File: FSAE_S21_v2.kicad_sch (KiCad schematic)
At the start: 56 parts

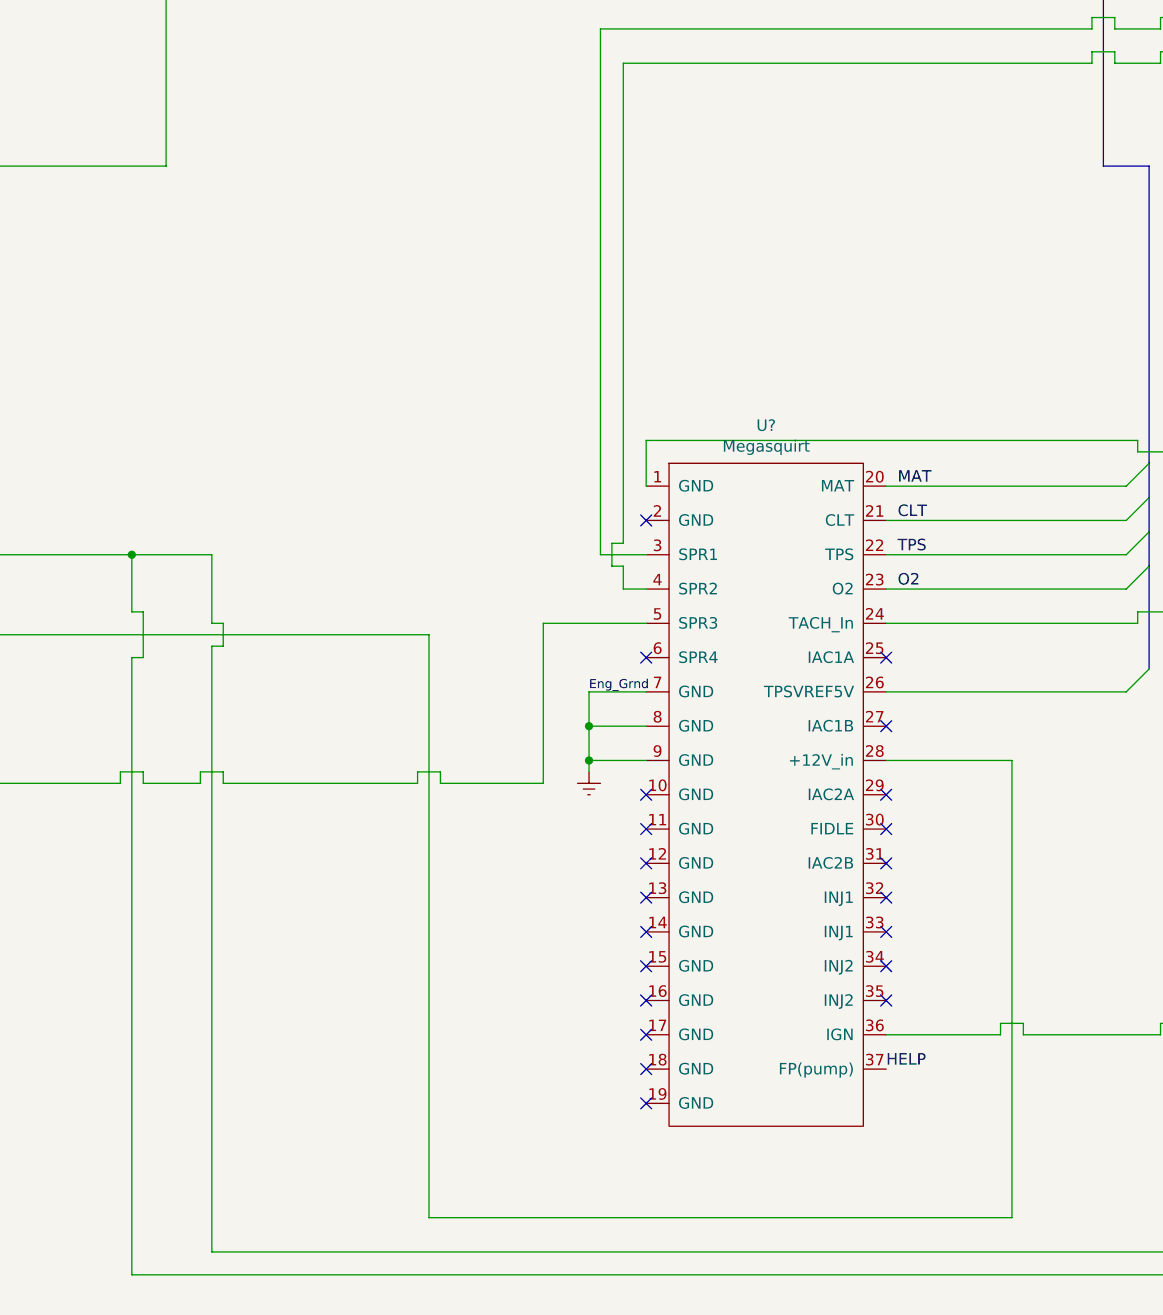
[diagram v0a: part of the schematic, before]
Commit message: Fixing pin 37
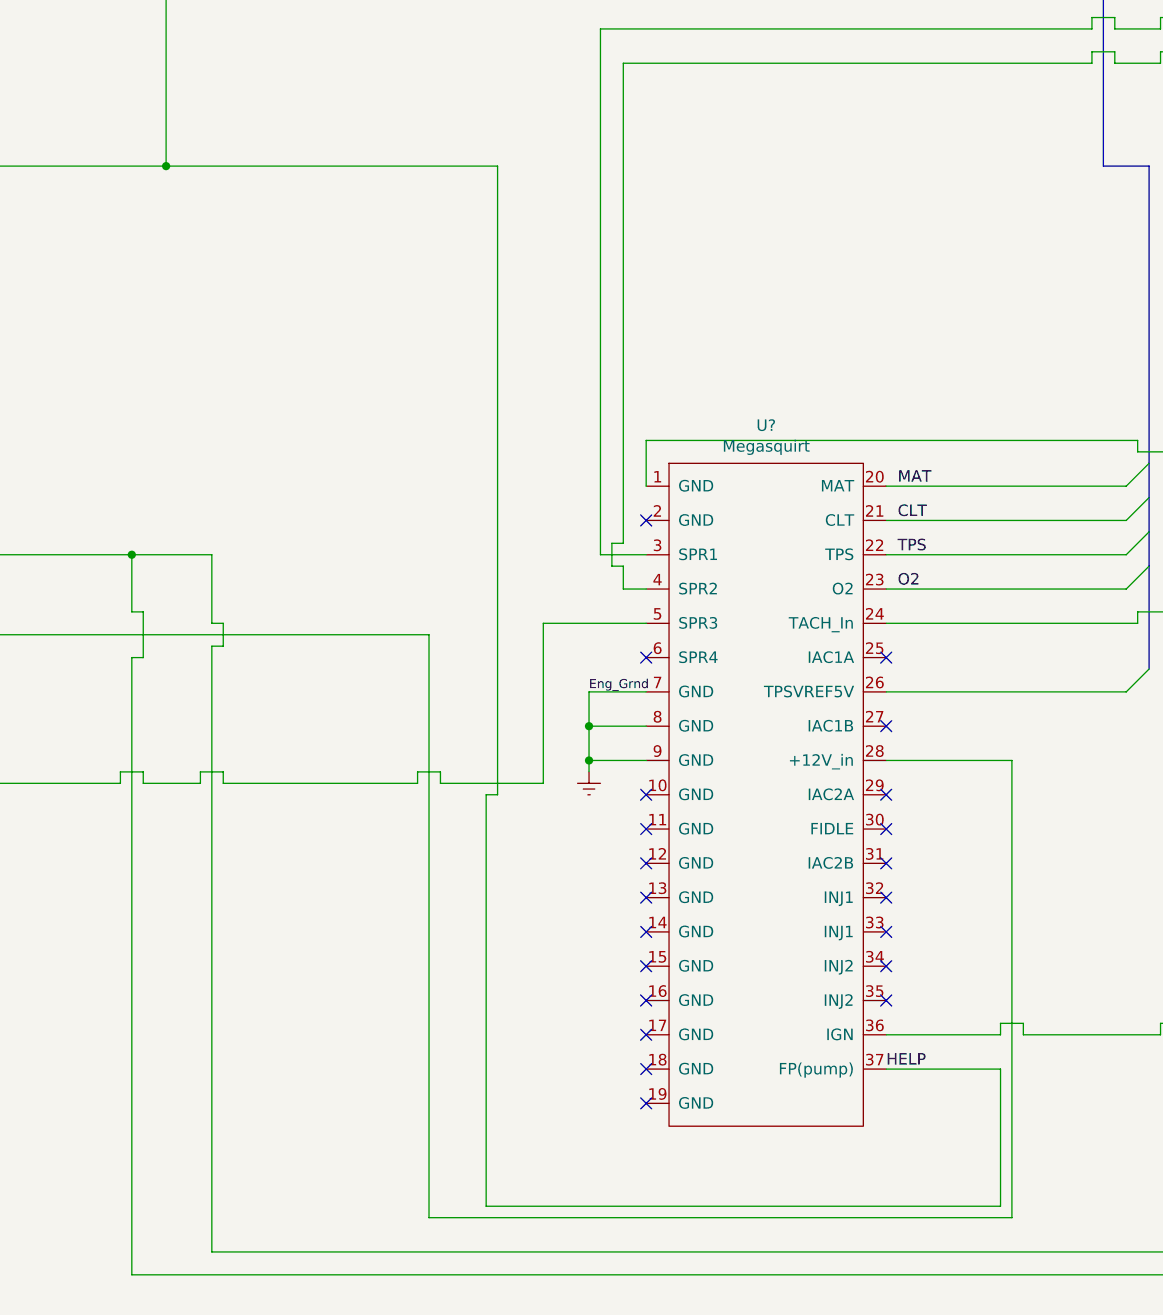
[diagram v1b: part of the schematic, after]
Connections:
- net HELP: now also SW?.2 (B)
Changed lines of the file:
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@@
   (junction (at 419.1 222.25) (diameter 0) (color 0 0 0 0)
+  )
+  (junction (at 251.46 130.81) (diameter 0) (color 0 0 0 0)
   )
   (junction (at 180.34 111.76) (diameter 0) (color 0 0 0 0)
@@
     (stroke (width 0) (type default) (color 0 0 0 0))
   )
+  (wire (pts (xy 331.47 231.14) (xy 344.17 231.14))
+    (stroke (width 0) (type default) (color 0 0 0 0))
+  )
   (bus (pts (xy 207.01 30.48) (xy 207.01 33.02))
     (stroke (width 0) (type default) (color 0 0 0 0))
@@
     (stroke (width 0) (type default) (color 0 0 0 0))
   )
+  (wire (pts (xy 287.02 200.66) (xy 288.29 200.66))
+    (stroke (width 0) (type default) (color 0 0 0 0))
+  )
   (wire (pts (xy 420.37 43.18) (xy 422.91 43.18))
     (stroke (width 0) (type default) (color 0 0 0 0))
@@
     (stroke (width 0) (type default) (color 0 0 0 0))
   )
+  (wire (pts (xy 344.17 246.38) (xy 287.02 246.38))
+    (stroke (width 0) (type default) (color 0 0 0 0))
+  )
   (wire (pts (xy 151.13 73.66) (xy 151.13 81.28))
     (stroke (width 0) (type default) (color 0 0 0 0))
@@
     (stroke (width 0) (type default) (color 0 0 0 0))
   )
+  (wire (pts (xy 288.29 130.81) (xy 288.29 200.66))
+    (stroke (width 0) (type default) (color 0 0 0 0))
+  )
   (wire (pts (xy 182.88 21.59) (xy 78.74 21.59))
     (stroke (width 0) (type default) (color 0 0 0 0))
@@
     (stroke (width 0) (type default) (color 0 0 0 0))
   )
+  (wire (pts (xy 344.17 231.14) (xy 344.17 246.38))
+    (stroke (width 0) (type default) (color 0 0 0 0))
+  )
   (wire (pts (xy 219.71 74.93) (xy 222.25 74.93))
     (stroke (width 0) (type default) (color 0 0 0 0))
@@
     (stroke (width 0) (type default) (color 0 0 0 0))
   )
+  (wire (pts (xy 287.02 246.38) (xy 287.02 200.66))
+    (stroke (width 0) (type default) (color 0 0 0 0))
+  )
   (wire (pts (xy 497.84 138.43) (xy 511.81 138.43))
     (stroke (width 0) (type default) (color 0 0 0 0))
@@
     (stroke (width 0) (type default) (color 0 0 0 0))
   )
+  (wire (pts (xy 288.29 130.81) (xy 251.46 130.81))
+    (stroke (width 0) (type default) (color 0 0 0 0))
+  )

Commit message: Some fixes
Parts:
- removed F?: Fuse (5 A), symbol Device:Fuse
- removed J?: ICM, symbol Connector:DB9_Female
- removed J?: MyChron 5 (EXP/PC), symbol Connector:DIN-5
- removed SW?: Starter Button, symbol Switch:SW_MEC_5G
- removed U?: IC1, symbol Device:IC
- removed U?: IC2, symbol Device:IC
- removed U?: IC3, symbol Device:IC
- removed U?: IC4, symbol Device:IC
- added J?: ICM, symbol Connector:DB9_Female
- added R?: 10k, symbol Device:R_US
- added SW?: Datalog Button, symbol Switch:SW_Push
- added SW?: Upshift Button, symbol Switch:SW_Push
- added SW?: Starter Button, symbol Switch:SW_MEC_5G
- added SW?: Downshift Button, symbol Switch:SW_Push
- added SW?: TC Button, symbol Switch:SW_Push
- added U?: IC3, symbol Device:IC
- added U?: IC2, symbol Device:IC
- added U?: DSS, symbol Device:IC
- added U?: IC4, symbol Device:IC
- added U?: USS, symbol Device:IC
- added U?: IC1, symbol Device:IC
- F?: value Fuse (????? A) -> Fuse (5 A)
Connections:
- net 12V: no longer F?.1, U?.1 (+12V_In)
- net Earth: now also U?.2 (GND), U?.3 (GND), J?.3, SW?.1, SW?.1 (A), SW?.2, SW?.2, SW?.2, SW?.2 (A); no longer K?.3, U?.35 (Spark_E)
- net TracCtrl: now also SW?.2
- net V_CKS: now also K?.5
- net V_PKS: now also U?.~ (VCC), U?.~ (VCC)
- net at F?.1: now also U?.~ (VCC), U?.~ (VCC), U?.~ (VCC), U?.~ (VCC)
- net at J?.2 (Pin_2): now also R?.2
- net at U?.24 (TACH_In): now also R?.1
- net at U?.30 (Datalog_in): now also SW?.1
- net Dshift_button renamed DS_Button
- net DS_Button: now also SW?.1
- net OPS renamed Oil Pres.
- net Oil Pres.: no longer U?.2 (IO)
- net OTS renamed Oil Temp
- net Ushift_button renamed US_Button
- net US_Button: now also SW?.1
- new net: K?.3, SW?.3 (B), SW?.4 (B)
- new net: F?.1, U?.1 (+12V_In)
- new net: J?.7, U?.~ (VCC)
- new net: J?.8, U?.~ (VCC)
- new net: J?.6, U?.~ (VCC)
- new net: J?.9, U?.~ (VCC)
- new net DS Solenoid: U?.~ (VCC)
- new net Oil Pressure: U?.2 (IO)
- new net US Solenoid: U?.~ (VCC)

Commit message: Some edits
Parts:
- removed F?: Fuse (5 A), symbol Device:Fuse
- removed U?: Injector Bank 2, symbol Device:Injector
- removed U?: Injector Bank 1, symbol Device:Injector
- removed U?: Injector Bank 3, symbol Device:Injector
- removed U?: Injector Bank 4, symbol Device:Injector
- added U?: Injector 3, symbol Device:Injector
- added U?: Injector 4, symbol Device:Injector
- added U?: BPS, Sensor:Aosong_DHT11_5.5x12.0_P2.54mm, symbol Sensor:DHT11
- added U?: Injector 1, symbol Device:Injector
- added U?: Injector 2, symbol Device:Injector
- added U?: FPS, Sensor:Aosong_DHT11_5.5x12.0_P2.54mm, symbol Sensor:DHT11
- F?: value Fuse (5 A) -> Fuse (10 A)
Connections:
- net +(pos): now also J?.2 (Pin_2), R?.2
- net -(neg): now also J?.1 (Pin_1), U?.1 (CRNK_GND)
- net Earth: no longer U?.7 (GND)
- net GND_Sensor: now also J?.2 (Pin_2), U?.7 (SNS_GND)
- net at F?.1: now also U?.1 (V+), U?.1 (V+), U?.1 (V+), U?.1 (V+)
- net at U?.18 (Sensor_Ground): now also U?.4 (GND), U?.4 (GND)
- net at U?.24 (MAP): now also U?.2 (IO)
- net at U?.26 (MAT): now also U?.2 (IO)
- net at U?.28 (TPS_VREF_5V): now also U?.1 (VCC), U?.1 (VCC)
- net HELP: no longer names the net of SW?.2 (B), U?.37 (Fuel)
- new net: F?.1, U?.~ (VCC), U?.~ (VCC), U?.~ (VCC), U?.~ (VCC)
- no-connect marks 67 -> 66

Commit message: More edits
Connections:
- net VCC_Sensor is gone; now on net 5V_REF: U?.1 (VCC), U?.1 (VCC)
- net 5V_REF: now reaches U?.1 (VCC)
- net 5V_REF: now also U?.1 (VCC)
- new net: F?.1, U?.~ (VCC), U?.~ (VCC), U?.~ (VCC), U?.~ (VCC)
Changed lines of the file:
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@@
   (junction (at 146.05 205.74) (diameter 0) (color 0 0 0 0)
   )
+  (junction (at 506.73 231.14) (diameter 0) (color 0 0 0 0)
+  )
   (junction (at 91.44 134.62) (diameter 0) (color 0 0 0 0)
   )
@@
     (stroke (width 0) (type default) (color 0 0 0 0))
   )
-  (bus_entry (at 487.68 224.79) (size 2.54 -2.54)
-    (stroke (width 0) (type default) (color 0 0 0 0))
-  )
   (bus_entry (at 494.03 222.25) (size 2.54 2.54)
     (stroke (width 0) (type default) (color 0 0 0 0))
@@
     (stroke (width 0) (type default) (color 0 0 0 0))
   )
+  (wire (pts (xy 495.3 231.14) (xy 487.68 231.14))
+    (stroke (width 0) (type default) (color 0 0 0 0))
+  )
   (wire (pts (xy 433.07 238.76) (xy 435.61 238.76))
     (stroke (width 0) (type default) (color 0 0 0 0))
@@
     (stroke (width 0) (type default) (color 0 0 0 0))
   )
+  (wire (pts (xy 506.73 224.79) (xy 506.73 231.14))
+    (stroke (width 0) (type default) (color 0 0 0 0))
+  )
   (wire (pts (xy 204.47 102.87) (xy 207.01 102.87))
     (stroke (width 0) (type default) (color 0 0 0 0))
@@
     (stroke (width 0) (type default) (color 0 0 0 0))
   )
-  (bus (pts (xy 490.22 222.25) (xy 494.03 222.25))
+  (wire (pts (xy 495.3 229.87) (xy 497.84 229.87))
     (stroke (width 0) (type default) (color 0 0 0 0))
   )
@@
     (stroke (width 0) (type default) (color 0 0 0 0))
   )
-  (wire (pts (xy 487.68 224.79) (xy 487.68 231.14))
+  (wire (pts (xy 506.73 231.14) (xy 497.84 231.14))
     (stroke (width 0) (type default) (color 0 0 0 0))
   )
@@
     (stroke (width 0) (type default) (color 0 0 0 0))
   )
+  (wire (pts (xy 497.84 229.87) (xy 497.84 231.14))
+    (stroke (width 0) (type default) (color 0 0 0 0))
+  )
   (wire (pts (xy 570.23 93.98) (xy 571.5 93.98))
     (stroke (width 0) (type default) (color 0 0 0 0))
@@
     (stroke (width 0) (type default) (color 0 0 0 0))
   )
+  (wire (pts (xy 461.01 224.79) (xy 461.01 248.92))
+    (stroke (width 0) (type default) (color 0 0 0 0))
+  )
   (wire (pts (xy 161.29 212.09) (xy 161.29 210.82))
     (stroke (width 0) (type default) (color 0 0 0 0))
@@
     (stroke (width 0) (type default) (color 0 0 0 0))
   )
-  (wire (pts (xy 461.01 224.79) (xy 461.01 248.92))
-    (stroke (width 0) (type default) (color 0 0 0 0))
-  )
   (bus (pts (xy 121.92 135.89) (xy 123.19 135.89))
     (stroke (width 0) (type default) (color 0 0 0 0))
@@
     (stroke (width 0) (type default) (color 0 0 0 0))
   )
+  (wire (pts (xy 495.3 231.14) (xy 495.3 229.87))
+    (stroke (width 0) (type default) (color 0 0 0 0))
+  )
   (wire (pts (xy 143.51 172.72) (xy 149.86 172.72))
     (stroke (width 0) (type default) (color 0 0 0 0))
@@
     (stroke (width 0) (type default) (color 0 0 0 0))
   )
-  (bus (pts (xy 481.33 222.25) (xy 490.22 222.25))
+  (bus (pts (xy 481.33 222.25) (xy 494.03 222.25))
     (stroke (width 0) (type default) (color 0 0 0 0))
   )
@@
     (stroke (width 0) (type default) (color 0 0 0 0))
   )
-  (wire (pts (xy 506.73 224.79) (xy 506.73 231.14))
-    (stroke (width 0) (type default) (color 0 0 0 0))
-  )
   (wire (pts (xy 260.35 115.57) (xy 260.35 173.99))
     (stroke (width 0) (type default) (color 0 0 0 0))
@@
     (effects (font (size 1.27 1.27)) (justify left bottom))
   )
+  (label "5V_REF" (at 499.11 231.14 0)
+    (effects (font (size 1.27 1.27)) (justify left bottom))
+  )
   (label "CLT" (at 435.61 227.33 0)
     (effects (font (size 1.27 1.27)) (justify left bottom))
@@
     (effects (font (size 1.27 1.27)) (justify left bottom))
   )
-  (label "GND_Sensor" (at 459.74 223.52 0)
+  (label "GND_Sensor" (at 461.01 228.6 0)
     (effects (font (size 1.27 1.27)) (justify left bottom))
   )
@@
     (effects (font (size 1.27 1.27)) (justify left bottom))
   )
-  (label "VCC_Sensor" (at 398.78 231.14 0)
+  (label "5V_REF" (at 398.78 231.14 0)
     (effects (font (size 1.27 1.27)) (justify left bottom))
   )

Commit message: made some more updates
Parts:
- removed F?: Fuse (15 A), symbol Device:Fuse
- removed F?: Fuse (10 A), symbol Device:Fuse
- removed F?: Fuse (50 A), symbol Device:Fuse
- removed F?: Fuse (3 A), symbol Device:Fuse
- removed J?: Rectifier, symbol Connector_Generic:Conn_02x03_Counter_Clockwise
- removed J?: AC Magneto, symbol Connector_Generic:Conn_01x03
- removed K?: Accessory Relay, Relay_THT:Relay_SPST_StandexMeder_SIL_Form1A, symbol Relay:SILxx-1Axx-71x
- added F?: Fuse (7.5 A), symbol Device:Fuse
- added F? (x2): Fuse (50 A), symbol Device:Fuse
- added F?: Fuse (5 A?), symbol Device:Fuse
- added F?: Fuse (20 A), symbol Device:Fuse
- added F?: Fuse (15 A), symbol Device:Fuse
- added F?: Fuse (10 A), symbol Device:Fuse
- added F?: Fuse (3 A), symbol Device:Fuse
- added J?: Rectifier, symbol Connector_Generic:Conn_02x03_Counter_Clockwise
- added J?: AC Magneto, symbol Connector_Generic:Conn_01x03
- added K?: Spark Relay, Relay_THT:Relay_SPST_StandexMeder_SIL_Form1A, symbol Relay:SILxx-1Axx-71x
- added U?: Camshaft P.S., Sensor:Aosong_DHT11_5.5x12.0_P2.54mm, symbol Sensor:DHT11
- F?: value Fuse (5 A) -> Fuse (5 A?)
- F?: value Fuse (15 A) -> Fuse (10 A)
- J?: value Arduino #1 -> Dash?
- K?: value Fuel/Spark Relay -> Fuel Relay
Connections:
- net Earth: now also K?.5, J?.1 (Pin_1)
- net V_CKS: now also F?.2
- net V_PKS: now also F?.2, F?.2, F?.2, F?.2, F?.2, F?.2; no longer K?.1, K?.1, K?.1, K?.1, U?.~ (VCC), U?.~ (VCC)
- net at F?.2, K?.7: now also F?.2
- net at K?.7: now also M?.1 (+) (x2)
- net at SW?.1 (A): now also F?.2; no longer BT?.1 (+)
- net at U?.1 (+12V_In): now also F?.1
- net CAM_Shaft: no longer names the net of U?.32 (Cam_input)
- new net: F?.1, K?.1 (x4)
- new net: BT?.1 (+), F?.1
- new net: F?.1, U?.~ (VCC), U?.~ (VCC), U?.~ (VCC), U?.~ (VCC)
- new net: F?.1, J?.3 (Pin_3)
- new net: J?.1 (Pin_1), J?.4 (Pin_4)
- new net: J?.2 (Pin_2), J?.5 (Pin_5)
- new net: J?.3 (Pin_3), J?.6 (Pin_6)
- new net: F?.1, U?.~ (VCC), U?.~ (VCC)
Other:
- note added: "NOTE: CHECK WITH LIGHT DATASHEET ABOUT FUSE RATING"
- note added: "NOTE: CHECK WITH MASON ABOUT FUSE RATING"
- note added: "NOTE: CHECK WITH PI/DISPLAY DATASHEET ABOUT FUSE RATING"
- note added: "NOTE: FIX PKS WIRING"
- note added: "Note: Add Raspberry Pi + CANBUS Connection for that"

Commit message: Added wiring colors and hall effects + other stuff
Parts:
- removed D?: Temperature LED, symbol Device:LED
- removed R?: 10k, symbol Device:R_US
- removed SW?: Fuel/Spark Switch, symbol Switch:SW_SPST
- removed SW?: Downshift Button, symbol Switch:SW_Push
- added F?: Fuse (20 A), symbol Device:Fuse
- added R?: 10k, symbol Device:R_US
- added RV?: FL LinPot, symbol Device:R_Potentiometer
- added RV?: FR LinPot, symbol Device:R_Potentiometer
- added RV?: RL LinPot, symbol Device:R_Potentiometer
- added RV?: Steering Wheel Angle, symbol Device:R_Potentiometer
- added RV?: RR LinPot, symbol Device:R_Potentiometer
- added SW?: TC Input, symbol Switch:SW_Push
- added SW?: Fuel/Spark Cutoff Switch, symbol Switch:SW_DPST
- added U?: RL Hall Effect, Sensor:Aosong_DHT11_5.5x12.0_P2.54mm, symbol Sensor:DHT11
- added U? (x3): RR Hall Effect, Sensor:Aosong_DHT11_5.5x12.0_P2.54mm, symbol Sensor:DHT11
- F?: value Fuse (50 A) -> Fuse (50 A?)
- SW?: value TC Button -> Downshift Button
- U?: value Megasquirt -> MS3
- U?: value DSS -> Downshift Sol.
- U?: value BPS -> Brake Pressure
- U?: value USS -> Upshift Sol.
- U?: value FPS -> Fuel Pressure
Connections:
- net DS Solenoid is gone; now on net Solenoid_+12v: U?.~ (VCC)
- net TracCtrl is gone; now on net DS_Button: SW?.2, U?.11 (Launch_in)
- net US Solenoid is gone; now on net US_Solenoid: U?.~ (VCC)
- net 5V_REF: now also U?.1 (VCC), U?.1 (VCC), U?.1 (VCC), U?.26 (5V_REF), U?.28 (5V_REF), RV?.1, RV?.1, RV?.1, RV?.1, RV?.1, U?.1 (VCC), U?.1 (VCC), U?.1 (VCC), U?.1 (VCC)
- net DS_Button: no longer U?.29 (Nitrous_in)
- net DS_Solenoid: now also U?.~ (VCC)
- net Earth: now also U?.10 (GND), U?.11 (GND), SW?.1; no longer SW?.2, SW?.2
- net GND_Sensor: now also U?.20 (GND_Sensor), U?.4 (GND), U?.4 (GND), U?.4 (GND), RV?.3, RV?.3, RV?.3, RV?.3, RV?.3, U?.4 (GND), U?.4 (GND), U?.4 (GND), U?.4 (GND)
- net Inj1: now also U?.2 (GND)
- net Inj2: now also U?.2 (GND)
- net Inj3: now also U?.2 (GND)
- net Inj4: now also U?.2 (GND)
- net MAP: no longer U?.23 (EXT_MAP)
- net Oil Pres.: now also U?.21 (SpareADC); no longer U?.22 (EGO2)
- net Oil Temp: now also U?.22 (EGO2); no longer U?.21 (SpareADC)
- net RL_Hall_Effect: now also U?.11 (SparkB(IGN1)), U?.2 (IO)
- net V_CKS: now also K?.3, K?.3; no longer K?.5
- net V_PKS: now also K?.1, F?.2; no longer K?.7
- net F/S Relay: now reaches K?.5
- net F/S Relay: now also K?.5, U?.37 (Fuel), SW?.1, SW?.2, SW?.3, SW?.4
- net at F?.2, F?.2, K?.7: no longer F?.2, F?.2
- net at M?.2 (-): now also K?.7; no longer K?.1
- net at SW?.3 (B), SW?.4 (B): now also K?.5; no longer K?.3
- net MS3X_12v: now reaches F?.1, U?.28 (+12V_IN)
- net O2_Output: now reaches J?.5 (Pin_5)
- net CRANK: now reaches U?.24 (CRANK)
- net CRANK: now also R?.1
- net CANH: now reaches U?.2 (CANH), U?.3 (CANH)
- net CANL: now reaches U?.3 (CANL), U?.4 (CANL)
- net DL_Button: now reaches SW?.1, U?.30 (Datalog_in)
- net CAM_Input: now reaches U?.32 (Cam_input)
- net CAM_Input: now also U?.2 (IO)
- net MicroSquirt_12v: now reaches F?.1, U?.1 (+12V_In)
- net RR_Hall_Effect: now reaches U?.12 (SparkA(IGN2))
- net RR_Hall_Effect: now also U?.2 (IO)
- net FR_Hall_Effect: now reaches U?.21 (VR2-)
- net FR_Hall_Effect: now also U?.2 (IO)
- net FPS: now reaches U?.2 (IO), U?.24 (MAP)
- net FL_LinPot: now reaches U?.25 (CLT)
- net BPS: now reaches U?.2 (IO), U?.26 (MAT)
- net FR_LinPot: now reaches U?.27 (TPS)
- net RL_LinPot: now reaches U?.29 (SPAREADC)
- net FL_Hall_Effect: now reaches U?.33 (VR1-)
- net FL_Hall_Effect: now also U?.2 (IO)
- net RR_LinPot: now reaches U?.34 (O2)
- net Steering_Wheel_Angle: now reaches U?.5 (SPARE_ADC2(MAF))
- net Steering_Wheel_Angle: now also RV?.2
- net TC: now reaches U?.6 (FLEX)
- net TC: now also SW?.2
- net Solenoid_+12v: now reaches F?.1, U?.~ (VCC), U?.~ (VCC)
- net at K?.1: now also F?.1
- net at K?.7: now also F?.2, F?.2
- net +(pos): no longer names the net of J?.2 (Pin_2)
- net +(pos): now also R?.2
- net -(neg) renamed CRANK_GND
- net O2 renamed O2_Input
- net WaterPump renamed WP_Relay
- new net: F?.1, U?.~ (VCC), U?.~ (VCC), U?.~ (VCC), U?.~ (VCC)
- new net: SW?.2, SW?.2
- new net MAP (Intake): U?.23 (EXT_MAP)
- now unconnected: U?.18 (Sensor_Ground)
- no-connect marks 66 -> 57
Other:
- note added: "NOTE: UPDATE PKS WIRING"
- note added: "Note: Can have grounds in Front/Rear/Cockpit/Engine"
- note added: "Note: Fuel controls both Spark and Fuel Relays"
- note removed: "NOTE: FIX PKS WIRING"
